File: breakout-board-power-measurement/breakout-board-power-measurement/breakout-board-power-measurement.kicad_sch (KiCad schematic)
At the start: 23 parts, among them U1 MCP3911A0-E/SS, U2 Si8641BA-B-IU, U3 ATA00BB36S-L

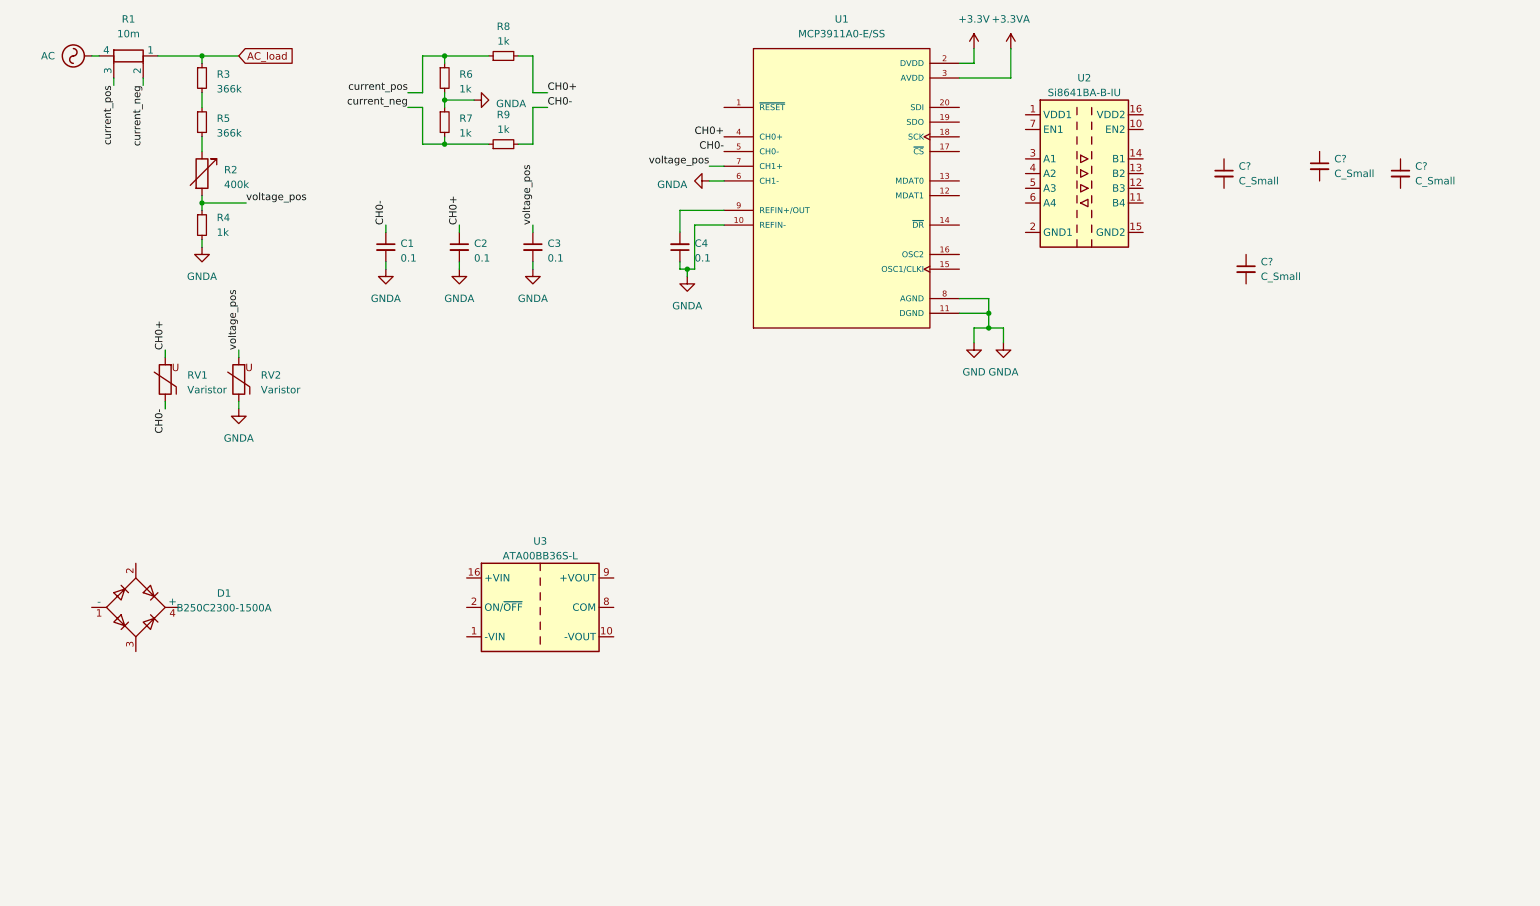
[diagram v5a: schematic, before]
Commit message: Major improvements: Power measurement schematic almost done.
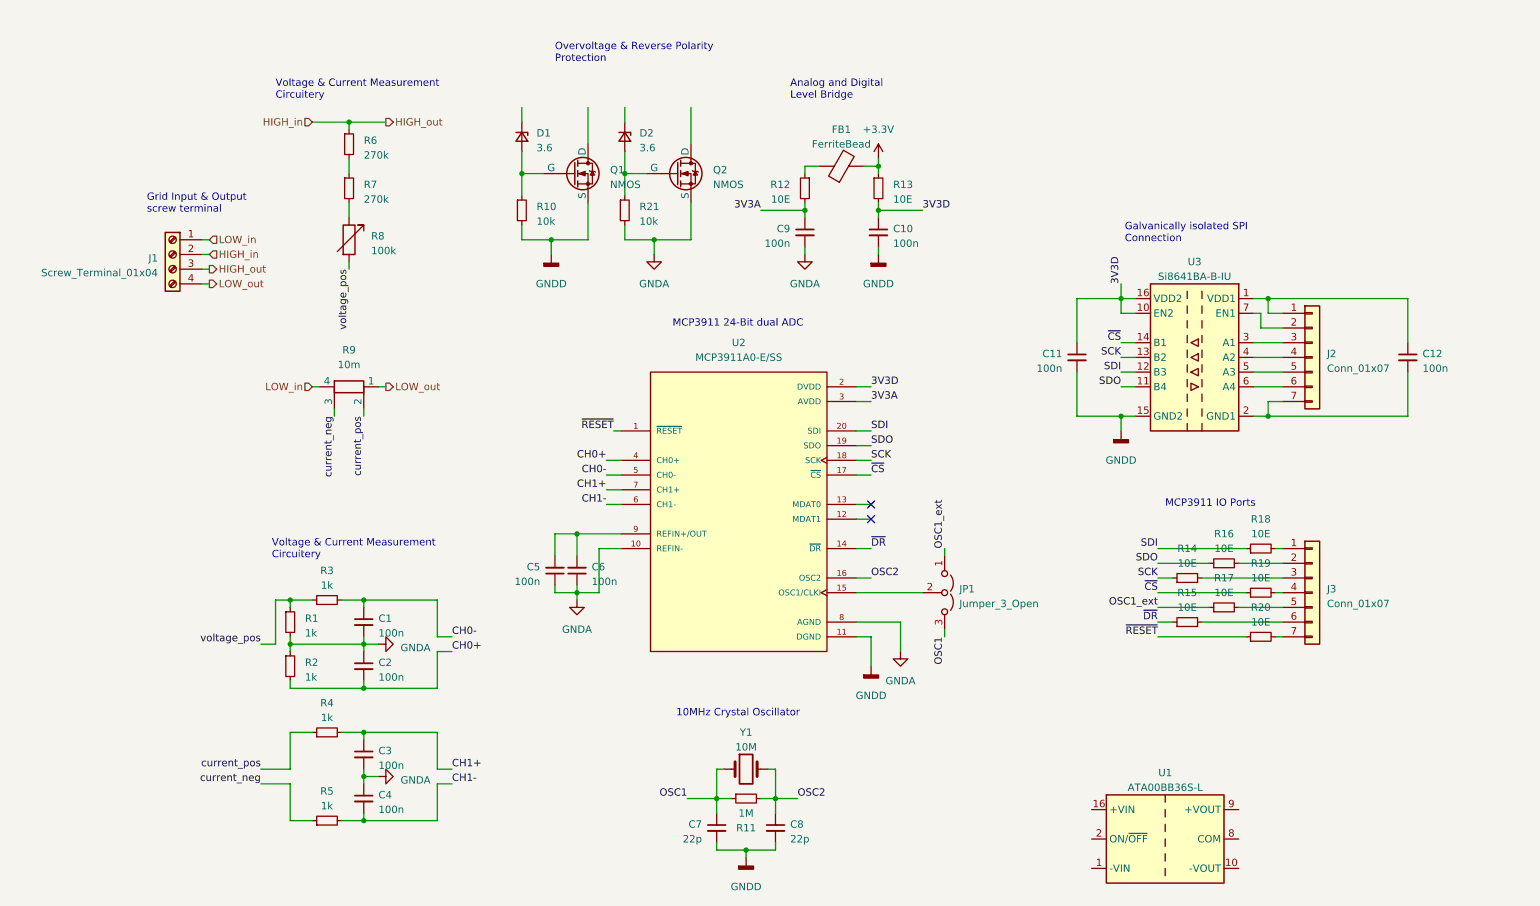
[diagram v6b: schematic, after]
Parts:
- removed C? (x4): C_Small, symbol Device:C_Small
- removed D1: B250C2300-1500A, Diode_THT:Diode_Bridge_19.0x3.5x10.0mm_P5.0mm, symbol Diode_Bridge:B250C2300-1500A
- removed R4, R6, R7: 1k, symbol Device:R_Small
- removed RV1, RV2: Varistor, symbol Device:Varistor
- added C10, C11, C12, C4, C6, C9: 100n, symbol Device:C_Small
- added C7, C8: 22p, symbol Device:C_Small
- added D1, D2: 3.6, symbol Device:D_Zener_Small
- added FB1: FerriteBead, symbol Device:FerriteBead
- added J1: Screw_Terminal_01x04, symbol Connector:Screw_Terminal_01x04
- added J2, J3: Conn_01x07, symbol Connector_Generic:Conn_01x07
- added JP1: Jumper_3_Open, symbol Jumper:Jumper_3_Open
- added Q1, Q2: NMOS, symbol Simulation_SPICE:NMOS
- added R1, R2, R3: 1k, symbol Device:R_Small
- added R10, R21: 10k, symbol Device:R_Small
- added R11: 1M, symbol Device:R_Small
- added R12, R13, R14, R15, R16, R17, R18, R19, R20: 10E, symbol Device:R_Small
- added Y1: 10M, symbol Device:Crystal
- C1, C2, C3: value 0.1 -> 100n
- C5: renamed from C4; value 0.1 -> 100n
- R6: renamed from R3; value 366k -> 270k
- R7: renamed from R5; value 366k -> 270k
- R8: renamed from R2; value 400k -> 100k
- renumbered R8 to R4, R9 to R5, R1 to R9, U3 to U1, U1 to U2, U2 to U3
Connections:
- net +3.3V: now also FB1.2, R13.1; no longer U2.2 (DVDD)
- net CH0+: now also C2.2, R2.2; no longer C2.1, R4.2
- net CH0-: now also R3.2; no longer R5.2
- net current_neg: now also R9.3; no longer R9.2
- net current_pos: now also R9.2; no longer R9.3
- net voltage_pos: now also R1.1, R3.1; no longer C3.1, U2.7 (CH1+)
- net at C5.2, U2.9 (REFIN+/OUT): now also C6.2
- net at U3.1 (VDD1): now also C12.1, J2.1 (Pin_1)
- net 3V3D: now reaches U3.10 (EN2)
- net 3V3D: now also U2.2 (DVDD), U3.16 (VDD2), C10.1, C11.1, R13.2
- net SDO: now reaches U3.11 (B4)
- net SDO: now also U2.19 (SDO), R16.1
- net SDI: now reaches U3.12 (B3)
- net SDI: now also U2.20 (SDI), R18.1
- net SCK: now reaches U3.13 (B2)
- net SCK: now also U2.18 (SCK), R14.1
- net ~{CS}: now reaches U3.14 (B1)
- net ~{CS}: now also U2.17 (~{CS}), R19.1
- net GNDD: now reaches U3.15 (GND2), U3.9 (GND2)
- net GNDD: now also U2.11 (DGND), C10.2, C11.2, C7.2, C8.2, Q1.3 (S), R10.2
- net at U3.2 (GND1), U3.8 (GND1): now also C12.2, J2.7 (Pin_7)
- net at U3.3 (A1): now also J2.3 (Pin_3)
- net at U3.4 (A2): now also J2.4 (Pin_4)
- net at U3.5 (A3): now also J2.5 (Pin_5)
- net at U3.6 (A4): now also J2.6 (Pin_6)
- net at U3.7 (EN1): now also J2.2 (Pin_2)
- net ~{RESET}: now reaches U2.1 (~{RESET})
- net ~{RESET}: now also R20.1
- net ~{DR}: now reaches U2.14 (~{DR})
- net ~{DR}: now also R15.1
- net at U2.15 (OSC1/CLKI): now also JP1.2 (C)
- net OSC2: now reaches U2.16 (OSC2)
- net OSC2: now also C8.1, R11.2, Y1.2
- net +3.3VA renamed 3V3A
- net 3V3A: now also C9.1, R12.2
- net AC renamed LOW_in
- net LOW_in: now also J1.1 (Pin_1)
- net AC_load renamed HIGH_in
- net HIGH_in: now also J1.2 (Pin_2), J1.3 (Pin_3); no longer R9.1
- net GND renamed GNDA
- net GNDA: now also C2.1, C4.1, C6.1, C9.2, Q2.3 (S), R1.2, R2.1, R21.2; no longer C2.2, U2.11 (DGND), U2.6 (CH1-)
- new net: D2.2 (A), Q2.2 (G), R21.1
- new net: FB1.1, R12.1
- new net: D1.2 (A), Q1.2 (G), R10.1
- new net: J3.1 (Pin_1), R18.2
- new net: J3.2 (Pin_2), R16.2
- new net: J3.3 (Pin_3), R14.2
- new net: J3.4 (Pin_4), R19.2
- new net: J3.5 (Pin_5), R17.2
- new net: J3.6 (Pin_6), R15.2
- new net: J3.7 (Pin_7), R20.2
- new net CH1+: C3.1, R4.2, U2.7 (CH1+)
- new net CH1-: C4.2, R5.2, U2.6 (CH1-)
- new net LOW_out: J1.4 (Pin_4), R9.1
- new net OSC1: C7.1, JP1.3 (B), R11.1, Y1.1
- new net OSC1_ext: JP1.1 (A), R17.1
- no-connect marks 0 -> 2
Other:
- note added: "10MHz Crystal Oscillator"
- note added: "Analog and Digital Level Bridge"
- note added: "Galvanically isolated SPI Connection"
- note added: "Grid Input & Output screw terminal"
- note added: "MCP3911 24-Bit dual ADC"
- note added: "MCP3911 IO Ports"
- note added: "Overvoltage & Reverse Polarity Protection"
- note added: "Voltage & Current Measurement Circuitery"
- moved on the sheet: C5, R4, R5, R6, R7, R8, R9, U1, U2, U3

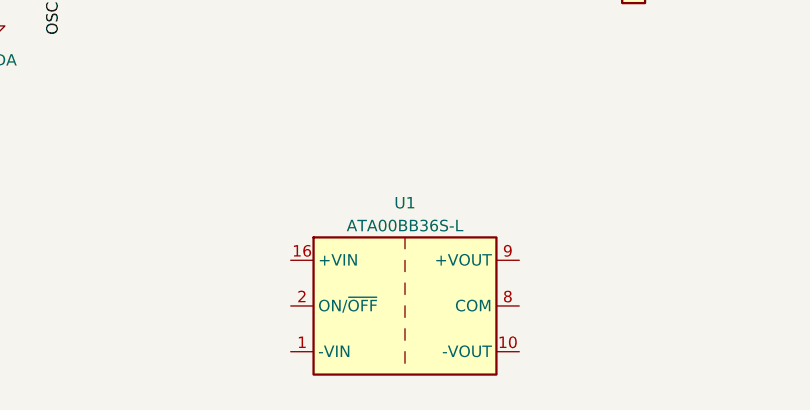
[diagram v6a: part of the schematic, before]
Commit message: Added breakout board for simple X-Cap power supply.
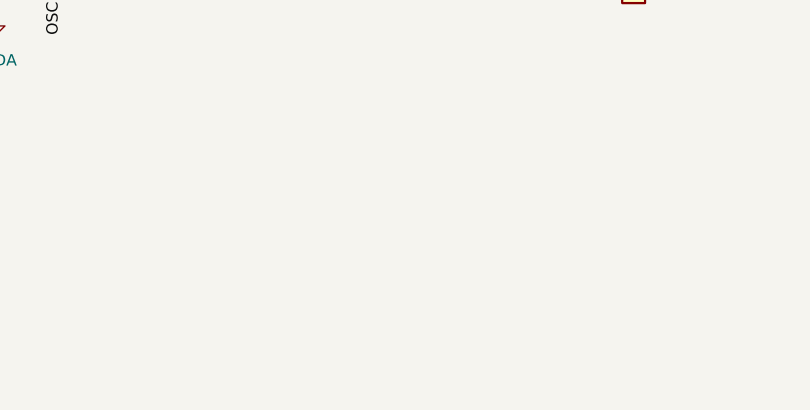
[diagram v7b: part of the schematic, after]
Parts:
- removed U1: ATA00BB36S-L, Converter_DCDC:Converter_DCDC_Artesyn_ATA_SMD, symbol Converter_DCDC:ATA00BB36S-L
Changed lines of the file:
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@@
-    )
-  )
-  (symbol (lib_id "Converter_DCDC:ATA00BB36S-L") (at 210.82 161.925 0) (unit 1)
-    (in_bom yes) (on_board yes) (dnp no) (fields_autoplaced)
-    (property "Reference" "U1" (at 210.82 150.495 0)
-      (effects (font (size 1.27 1.27)))
-    )
-    (property "Value" "ATA00BB36S-L" (at 210.82 153.035 0)
-      (effects (font (size 1.27 1.27)))
-    )
-    (property "Footprint" "Converter_DCDC:Converter_DCDC_Artesyn_ATA_SMD" (at 210.82 170.815 0)
-      (effects (font (size 1.27 1.27) italic) hide)
-    )
-    (property "Datasheet" "https://www.artesyn.com/power/assets/ata_series_ds_01apr2015_79c25814fd.pdf" (at 210.82 173.355 0)
-      (effects (font (size 1.27 1.27)) hide)
-    )
-    (pin "1")
-    (pin "10")
-    (pin "16")
-    (pin "2")
-    (pin "7")
-    (pin "8")
-    (pin "9")
-    (instances
-      (project "breakout-board-power-measurement"
-        (path "/433e477a-c382-4a77-a1aa-b42c4a1fe28b"
-          (reference "U1") (unit 1)
-        )
-      )
     )
   )

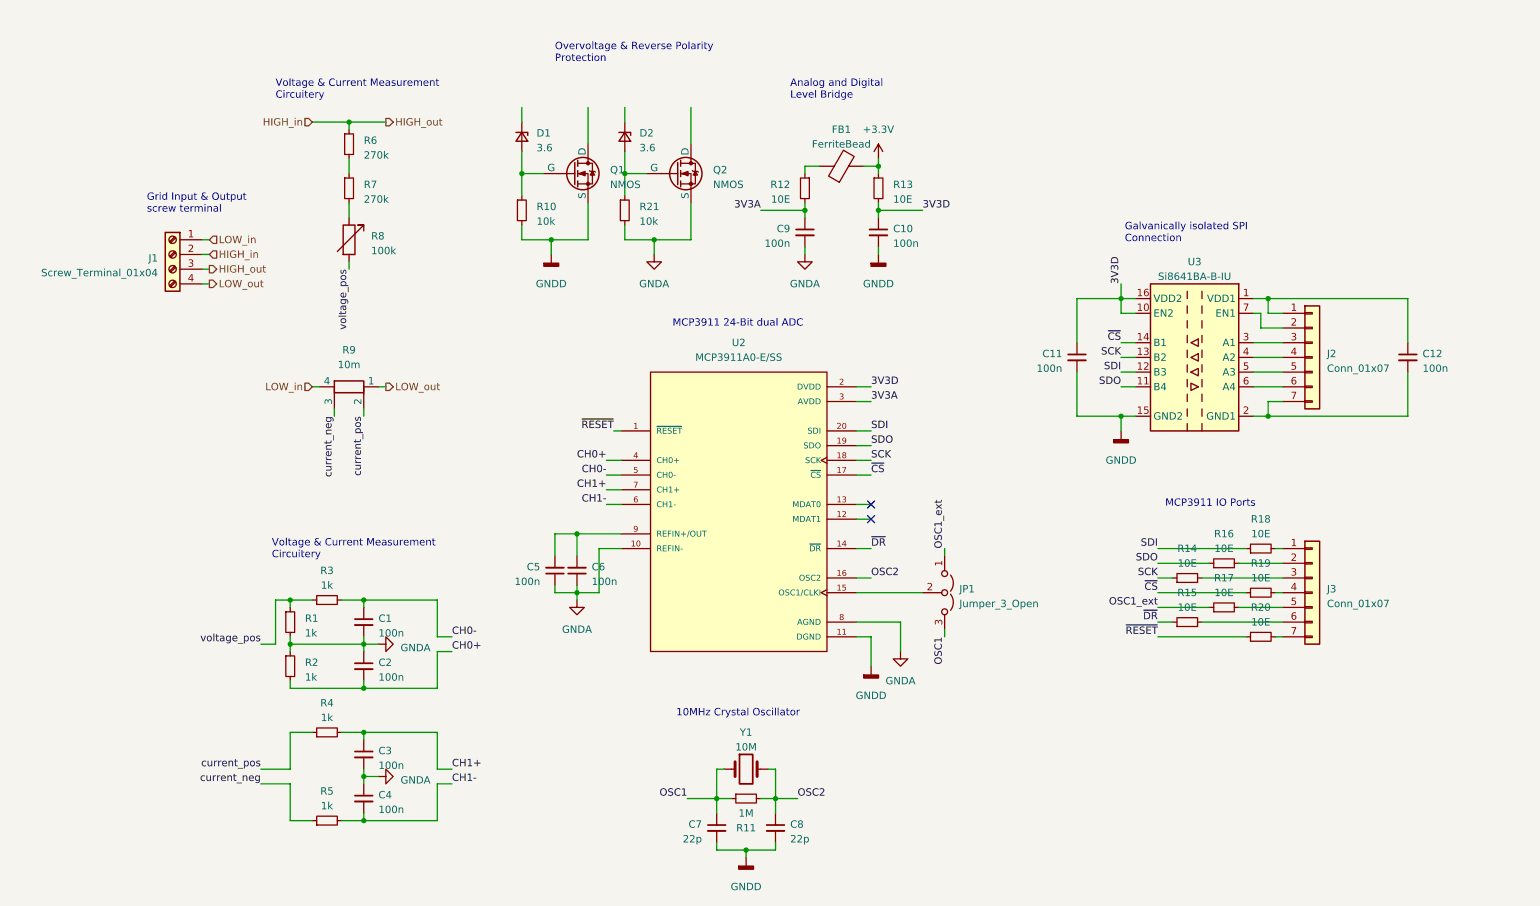
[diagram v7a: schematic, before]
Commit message: Safety circuit and x-cap psu circuit added.
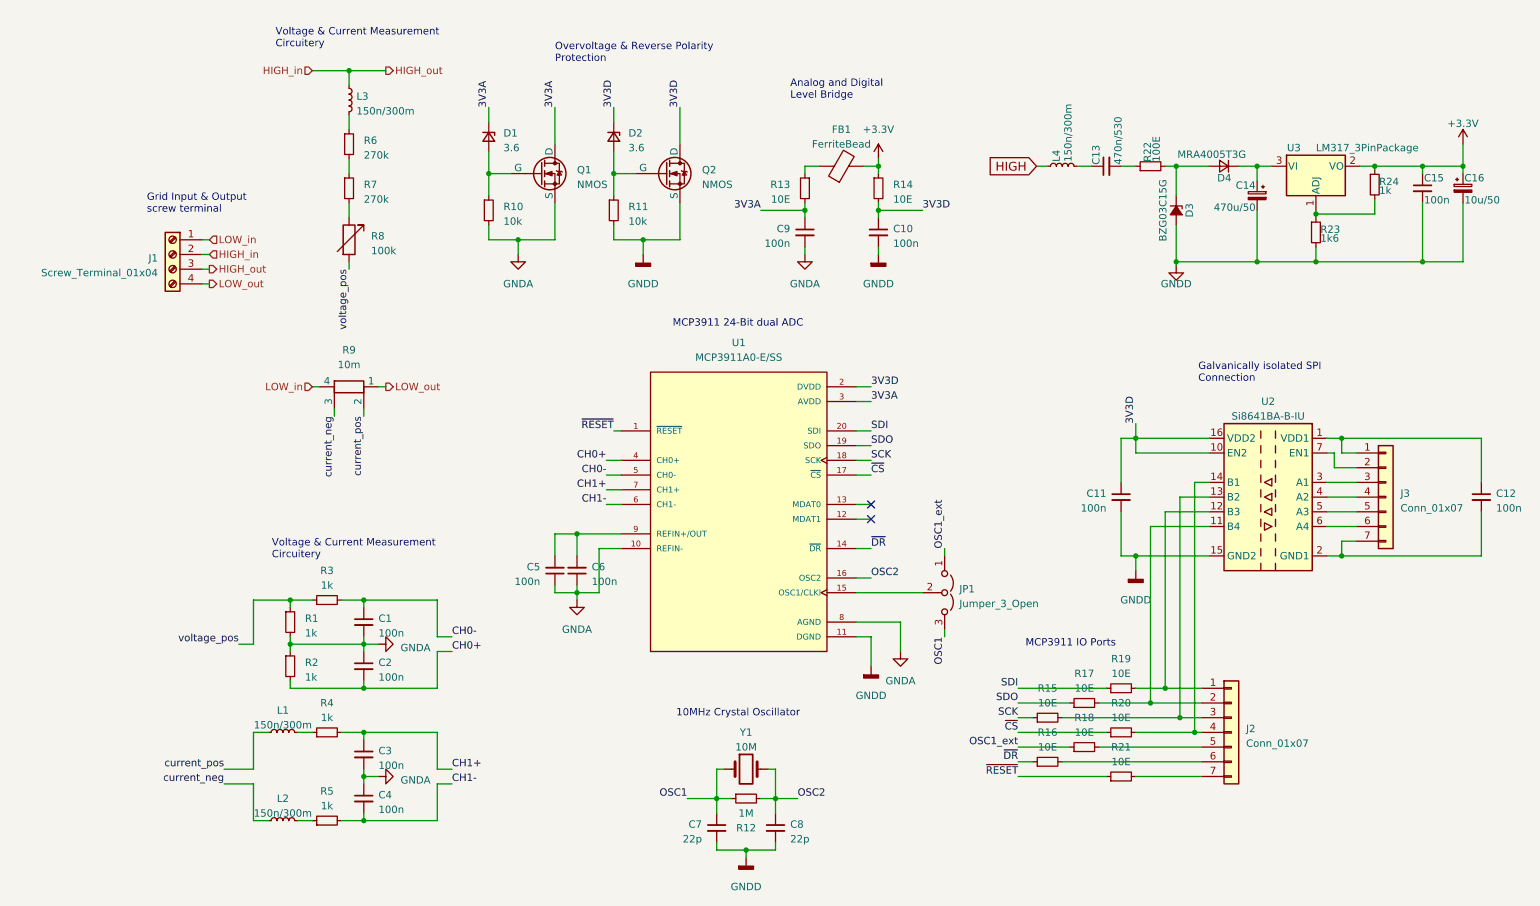
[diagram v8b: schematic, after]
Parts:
- added C13: 470n/530, Capacitors_THT:C_Rect_L26.5mm_W10.5mm_P22.50mm_MKS4, symbol Power-Analyzer-rescue:C_Small
- added C14: 470u/50, Capacitors_Tantalum_SMD:CP_Tantalum_Case-D_EIA-7343-31_Hand, symbol Power-Analyzer-rescue:CP_Small
- added C15: 100n, Capacitors_SMD:C_1206_HandSoldering, symbol Power-Analyzer-rescue:C_Small
- added C16: 10u/50, Capacitors_Tantalum_SMD:CP_Tantalum_Case-D_EIA-7343-31_Hand, symbol Power-Analyzer-rescue:CP_Small
- added D3: BZG03C15G, Diodes_SMD:D_SMA-SMB_Universal_Handsoldering, symbol Power-Analyzer-rescue:D_Zener_Small_ALT
- added D4: MRA4005T3G, Diodes_SMD:D_SMA-SMB_Universal_Handsoldering, symbol Power-Analyzer-rescue:D_Small
- added L1, L2, L3: 150n/300m, symbol Device:L_Small
- added L4: 150n/300m, Inductors_SMD:L_1206_HandSoldering, symbol Power-Analyzer-rescue:L_Small
- added R22: 100E, Resistors_SMD:R_1206_HandSoldering, symbol Power-Analyzer-rescue:R_Small
- added R23: 1k6, Resistors_SMD:R_1206_HandSoldering, symbol Power-Analyzer-rescue:R_Small
- added R24: 1k, Resistors_SMD:R_1206_HandSoldering, symbol Power-Analyzer-rescue:R_Small
- added U3: LM317_3PinPackage, TO_SOT_Packages_SMD:SOT-89-3_Handsoldering, symbol Power-Analyzer-rescue:LM317_3PinPackage
- renumbered D2 to D1, D1 to D2, J3 to J2, J2 to J3, Q2 to Q1, Q1 to Q2, R21 to R10, R10 to R11, R11 to R12, R12 to R13, R13 to R14, R14 to R15, R15 to R16, R16 to R17, R17 to R18, R18 to R19, R19 to R20, R20 to R21, U2 to U1, U3 to U2
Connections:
- net 3V3A: now also D1.1 (K), Q1.1 (D)
- net 3V3D: now also D2.1 (K), Q2.1 (D)
- net GNDD: now also C14.2, C15.2, C16.2, D3.2 (A), R23.2
- net HIGH_in: now also L3.1; no longer R6.1
- net SCK: no longer U2.13 (B2)
- net SDI: no longer U2.12 (B3)
- net SDO: no longer U2.11 (B4)
- net current_neg: now also L2.1; no longer R5.1
- net current_pos: now also L1.1; no longer R4.1
- net ~{CS}: no longer U2.14 (B1)
- net at J2.1 (Pin_1), R19.2: now also U2.12 (B3)
- net at J2.2 (Pin_2), R17.2: now also U2.11 (B4)
- net at J2.3 (Pin_3), R15.2: now also U2.13 (B2)
- net at J2.4 (Pin_4), R20.2: now also U2.14 (B1)
- new net: R23.1, R24.2, U3.1 (ADJ)
- new net: C14.1, D4.1 (K), U3.3 (VI)
- new net: L1.2, R4.1
- new net: L3.2, R6.1
- new net: C13.2, R22.1
- new net: D3.1 (K), D4.2 (A), R22.2
- new net: L2.2, R5.1
- new net: C13.1, L4.2
- new net +3V3: C15.1, C16.1, R24.1, U3.2 (VO)
- new net HIGH: L4.1
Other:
- moved on the sheet: C11, C12, D1, D2, J2, J3, Q1, Q2, R10, R11, R15, R16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
